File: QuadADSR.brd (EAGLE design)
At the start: 33.6 x 100 mm, 63 parts, among them IC1 74AC32D, IC5 MCP6004D, Q1 20MHz, T1 2N3904, T2 2N3904, T3 2N3904, T4 2N3904, U1 ATMEGA328P, U2 DUAL_OPAMP, U3 7805

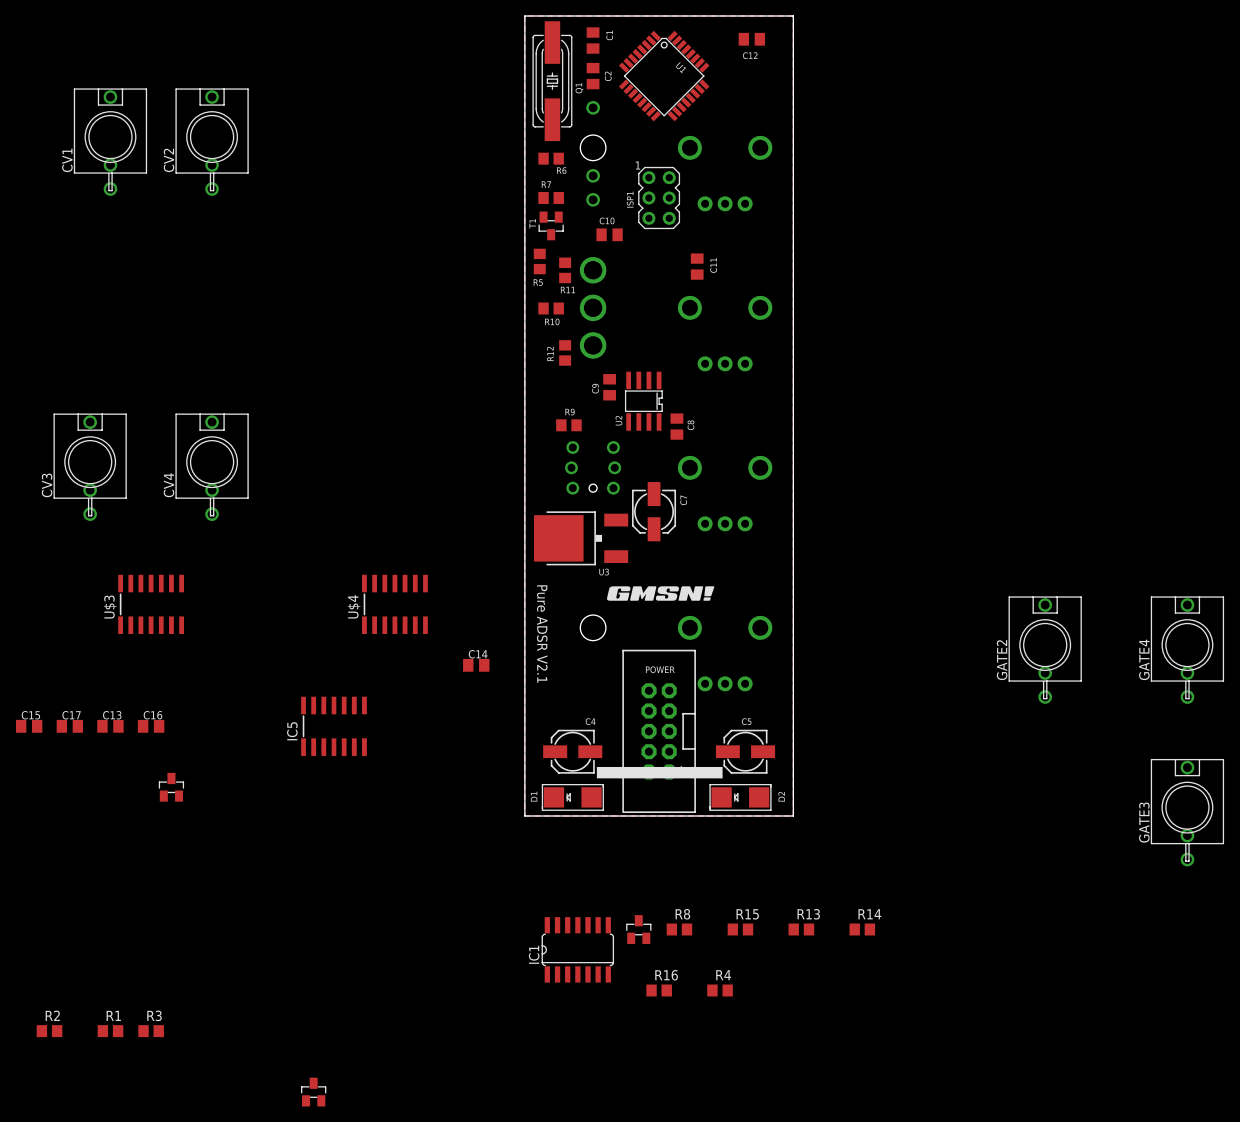
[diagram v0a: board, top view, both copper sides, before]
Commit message: Layed out board with shape pots
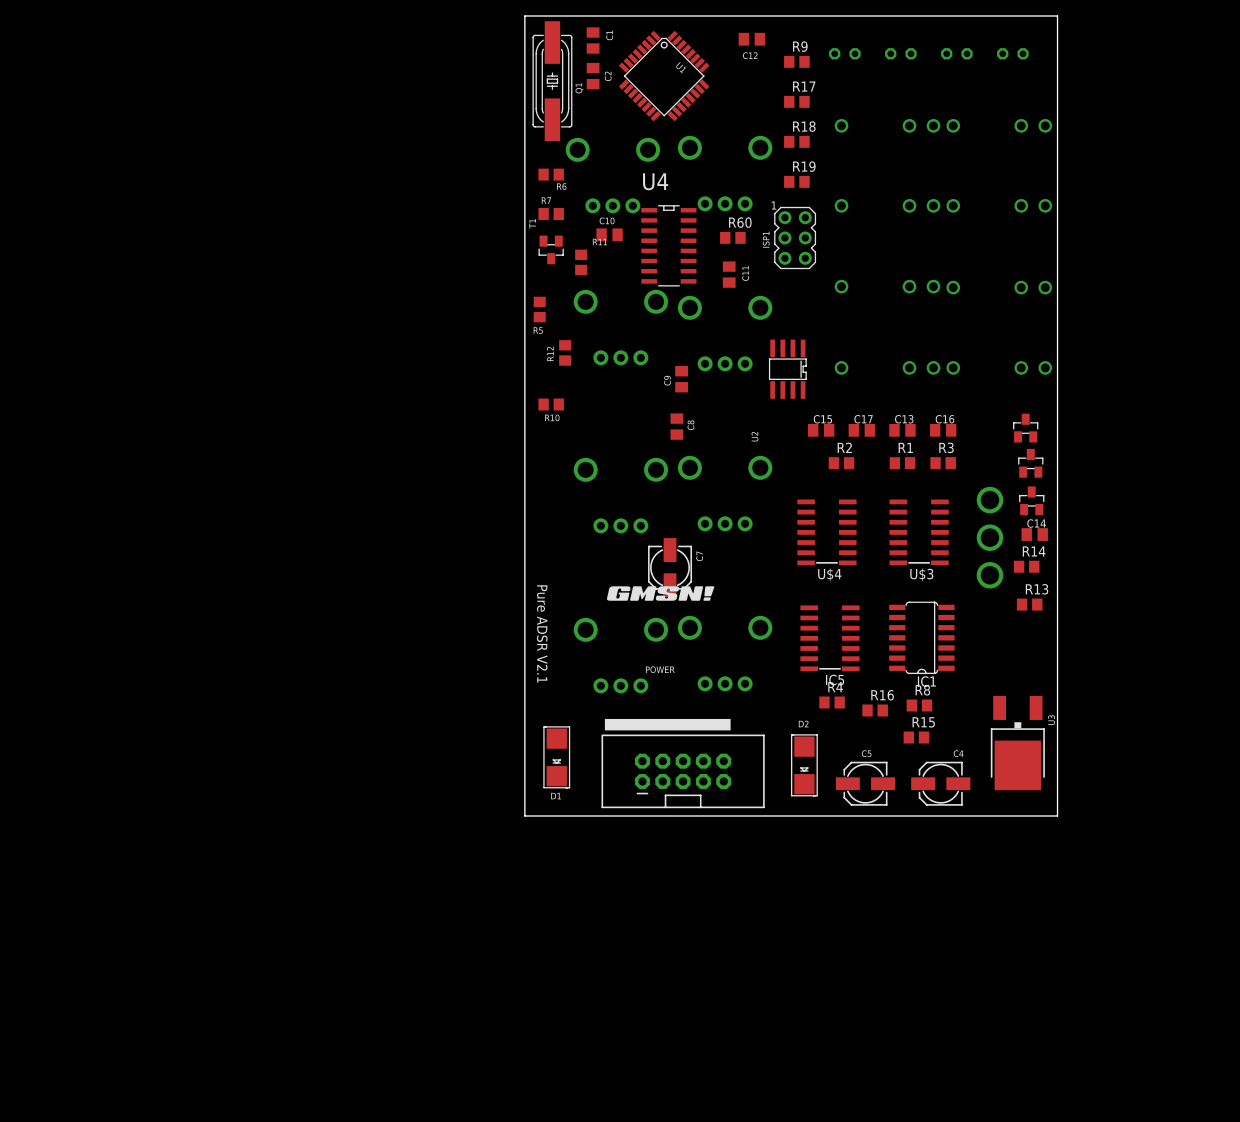
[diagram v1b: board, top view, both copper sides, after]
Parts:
- removed BUT: PB6149L-5, INSTRUO:PB6149L
- added D3: Red, led:LED5MM
- added D4: Green, led:LED5MM
- added D5: BLue, led:LED5MM
- added D6: Yellow, led:LED5MM
- added POT_SA, POT_SD, POT_SR, POT_ST: (no value), INSTRUO:Q-POT
- added R17, R18, R19: (no value), resistor:R0805
- added R60: 200K, rcl:R0805
- added U4: 4051, INSTRUO:N2222_ARRAY
- R9: value 10K -> (none); device rcl:R0805 -> resistor:R0805
- moved R1 121.8 mm to (48.2, 60.8)
- moved R2 121.8 mm to (40.6, 60.8)
- moved R3 121.8 mm to (53.3, 60.8)
- moved T3 121.7 mm to (63.6, 65.2)
- moved T2 113.3 mm to (64.4, 56.1)
- moved C13 105.7 mm to (48.2, 64.9)
- moved C15 105.7 mm to (38.0, 64.9)
- moved C16 105.7 mm to (53.3, 64.9)
- moved C17 105.7 mm to (43.1, 64.9)
- moved CV3 101.3 mm to (45.6, 82.9), flipped to the bottom, turned to 270 degrees
- moved U$3 96.4 mm to (50.3, 52.2), turned to 90 degrees
- moved CV1 96.4 mm to (45.6, 103.0), flipped to the bottom, turned to 270 degrees
- moved CV4 84.5 mm to (45.6, 72.7), flipped to the bottom, turned to 270 degrees
- moved CV2 84.1 mm to (45.6, 93.0), flipped to the bottom, turned to 270 degrees
- moved T4 76.1 mm to (64.2, 60.8)
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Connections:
- removed net B_TRIG: BUT.1, BUT.2, R9.1, U1.1, U1.2
- new net AIN: R60.1, U1.26
- new net LED_A: R9.2, U1.30
- new net LED_B: R17.2, U1.31
- new net LED_C: R18.2, U1.1
- new net LED_D: R19.2, U1.2
- new net N$19: D3.A, R9.1
- new net N$20: D4.A, R17.1
- new net N$21: D5.A, R18.1
- new net N$22: D6.A, R19.1
- new net N$69: R60.2, U4.3
- new net POT_SA: POT_SA.P$2, U4.1
- new net POT_SD: POT_SD.P$2, U4.5
- new net POT_SR: POT_SR.P$2, U4.4
- new net POT_ST: POT_ST.P$2, U4.2
- new net S0: U1.23, U4.11
- new net S1: U1.24, U4.10
- new net S2: U1.25, U4.9
- net +5V: now also POT_SA.P$3, POT_SD.P$3, POT_SR.P$3, POT_ST.P$3, U4.16; no longer R9.2
- net GND: now also D3.K, D4.K, D5.K, D6.K, POT_SA.P$1, POT_SD.P$1, POT_SR.P$1, POT_ST.P$1, U4.6, U4.7, U4.8; no longer BUT.3, BUT.4
- net POT_A: now also U4.13
- net POT_D: now also U4.14
- net POT_R: now also U4.12
- net POT_S: now also U4.15
- net TRIG1: now also U1.27; no longer U1.23
- net TRIG2: now also U1.28; no longer U1.24
- net TRIG3: now also U1.19; no longer U1.25
- net TRIG4: now also U1.22; no longer U1.26
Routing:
- removed copper zone on layer 1, net GND
- removed copper zone on layer 16, net GND
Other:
- board size 33.6 x 100 mm -> 66.6 x 100 mm

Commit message: Moved a few thigs round
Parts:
- moved U$2 10.2 mm to (9.37, 49.5)
- moved U2 5.68 mm to (31.3, 67.5)
- moved IC5 2.54 mm to (41.7, 38.9)
- moved U$4 2.54 mm to (41.3, 52.2)
- moved POT_SD 1.41 mm to (12.0, 80.0)
- moved C7 1.27 mm to (19.1, 49.0)
- moved C8 1.27 mm to (18.7, 65.4)
- moved C9 1.27 mm to (19.3, 71.3)
- moved POT_SR 1.00 mm to (12.0, 60.0)
- moved POT_ST 1.00 mm to (12.0, 40.0)
- moved U4 1.00 mm to (19.0, 87.0)
- moved POT_A 0.25 mm to (26.0, 100.0)
- moved POT_D 0.25 mm to (26.0, 80.0)
- moved POT_R 0.25 mm to (26.0, 40.0)
- moved POT_S 0.25 mm to (26.0, 60.0)

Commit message: Moved a few thigs round
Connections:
- removed net 3VREF: U$3.11, U$3.13, U$4.11, U$4.13
- removed net N$16: IC1.7
- removed net N$17: IC1.14
- net +5V: now also C15.1, IC1.14, IC5.4, U$3.1, U$3.11, U$3.13, U$4.1, U$4.11, U$4.13, U$4.9
- net 5V: no longer C15.1, IC5.4, U$3.1, U$4.1, U$4.9
- net GND: now also IC1.7
- net TRIG: no longer U1.9
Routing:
- net GND: track 0.00 -> 569.5 mm, vias 0 -> 13
- net +5V: track 0.00 -> 364.9 mm, vias 0 -> 12
- net TRIG3: track 0.00 -> 260.2 mm, vias 0 -> 9
- net TRIG1: track 0.00 -> 178.6 mm, vias 0 -> 5
- net CS1: track 0.00 -> 168.0 mm, vias 0 -> 4
- net T2: track 0.00 -> 161.0 mm, vias 0 -> 5
- net TRIG4: track 0.00 -> 153.9 mm, vias 0 -> 5
- net +12V: track 0.00 -> 144.1 mm, vias 0 -> 3
- net N$12: track 0.00 -> 143.3 mm, vias 0 -> 3
- net TRIG2: track 0.00 -> 139.0 mm, vias 0 -> 10
- net T1: track 0.00 -> 116.8 mm, vias 0 -> 5
- net N$6: track 0.00 -> 110.2 mm, vias 0 -> 6
- net TRIG: track 0.00 -> 107.3 mm, vias 0 -> 4
- net POT_ST: track 0.00 -> 102.7 mm
- net MOSI: track 0.00 -> 96.9 mm, vias 0 -> 2
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
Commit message: reroute
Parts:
- moved U$1 40.7 mm to (58.1, 20.3)
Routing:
- net GND: track 569.5 -> 0.00 mm, vias 13 -> 0
- net +5V: track 364.9 -> 0.00 mm, vias 12 -> 0
- net TRIG3: track 260.2 -> 0.00 mm, vias 9 -> 0
- net TRIG1: track 178.6 -> 0.00 mm, vias 5 -> 0
- net CS1: track 168.0 -> 0.00 mm, vias 4 -> 0
- net T2: track 161.0 -> 0.00 mm, vias 5 -> 0
- net TRIG4: track 153.9 -> 0.00 mm, vias 5 -> 0
- net +12V: track 144.1 -> 0.00 mm, vias 3 -> 0
- net N$12: track 143.3 -> 0.00 mm, vias 3 -> 0
- net TRIG2: track 139.0 -> 0.00 mm, vias 10 -> 0
- net T1: track 116.8 -> 0.00 mm, vias 5 -> 0
- net N$6: track 110.2 -> 0.00 mm, vias 6 -> 0
- net TRIG: track 107.3 -> 0.00 mm, vias 4 -> 0
- net POT_ST: track 102.7 -> 0.00 mm
- net MOSI: track 96.9 -> 0.00 mm, vias 2 -> 0
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
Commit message: updated Graphics
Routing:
- net GND: track 0.00 -> 615.4 mm, vias 0 -> 16
- net +5V: track 0.00 -> 400.6 mm, vias 0 -> 10
- net TRIG1: track 0.00 -> 162.2 mm, vias 0 -> 5
- net TRIG3: track 0.00 -> 155.0 mm, vias 0 -> 4
- net T2: track 0.00 -> 148.1 mm, vias 0 -> 5
- net TRIG2: track 0.00 -> 143.2 mm, vias 0 -> 6
- net N$18: track 0.00 -> 138.7 mm
- net +12V: track 0.00 -> 138.5 mm, vias 0 -> 3
- net CS1: track 0.00 -> 133.8 mm, vias 0 -> 6
- net TRIG4: track 0.00 -> 125.1 mm, vias 0 -> 7
- net N$12: track 0.00 -> 114.1 mm, vias 0 -> 3
- net MOSI: track 0.00 -> 107.2 mm, vias 0 -> 4
- net TRIG: track 0.00 -> 104.2 mm, vias 0 -> 2
- net T1: track 0.00 -> 103.1 mm, vias 0 -> 9
- net POT_ST: track 0.00 -> 101.5 mm
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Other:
- board text added: "Attack Shape"
- board text added: "Decay Shape"
- board text added: "Pure Quad ADSR PCB1"
- board text added: "RELEASE Shape"
- board text added: "Sustain Time"
- board text added: "copyright GMSN Ltd Andy C 2018"
- board text removed: "TRIGGER BUTTON"
- board text removed: "copyright GMSN Ltd 2016"
